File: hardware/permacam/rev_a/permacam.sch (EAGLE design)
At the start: 89 parts, among them J1 TC2030-JLINK-NL, Q1 PMDXB950UPEL, Q3 PMDXB950UPEL, Q5 PMDXB950UPEL, Q6 PMDXB950UPEL, U1 AB1815-T3, U10 NRF52840, U2 BQ25505, U3 EKMB1101111, U4 HM01B0-ANA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

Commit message: clean and orient design blocks
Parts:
- added C17, C18, C19: 0.1uF, passives:CAPACITOR0402_CAP
- added C20: 10uF, passives:CAPACITOR0603_CAP
- added R5, R6: 1k, passives:RESISTOR0402_RES
- added U5: MCP1810, chips:MCP1810
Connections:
- new net !CAM_EN: U5.!SHDN
- new net CAM_D0: U10.P0.22, U4.D0
- new net CAM_D1: U4.D1
- new net CAM_D2: U4.D2
- new net CAM_D3: U4.D3
- new net CAM_INT: U10.P1.03, U4.INT
- new net CAM_SCL: U10.P0.11
- new net CAM_SDA: R5.2, R6.2, U10.P0.07, U4.SCL, U4.SDA
- new net CAM_TRIG: U10.P1.02, U4.TRIG
- new net FVLD: U10.P0.24, U4.FVLD
- new net LVLD: U10.P0.23, U4.LVLD
- new net MCLK: U10.P0.20, U4.MCLK
- new net PCLKO: U10.P0.21, U4.PCLKO
- new net VCC28: C17.1, C18.1, C19.1, C20.1, R5.1, R6.1, U4.AVDD, U4.DVDD, U4.IOVDD, U5.VOUT
- net !LT_EN: now also U10.P1.01; no longer U10.P0.24
- net GND: now also C17.2, C18.2, C19.2, C20.2, U4.GND, U5.GND
- net VCC: now also U5.VIN
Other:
- moved on the sheet: U4

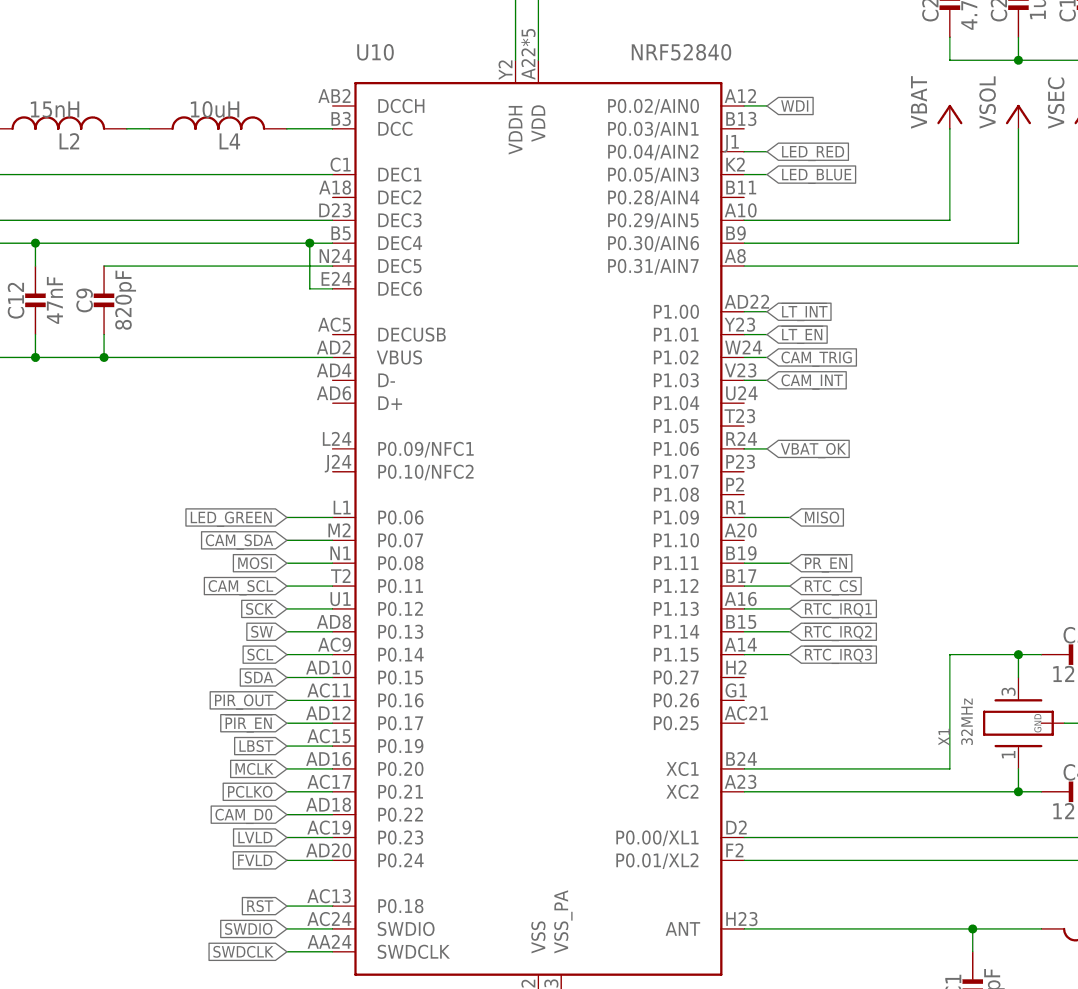
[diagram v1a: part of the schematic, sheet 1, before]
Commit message: Route signals on board - no airwires or major drc
Need to add optional MSP430
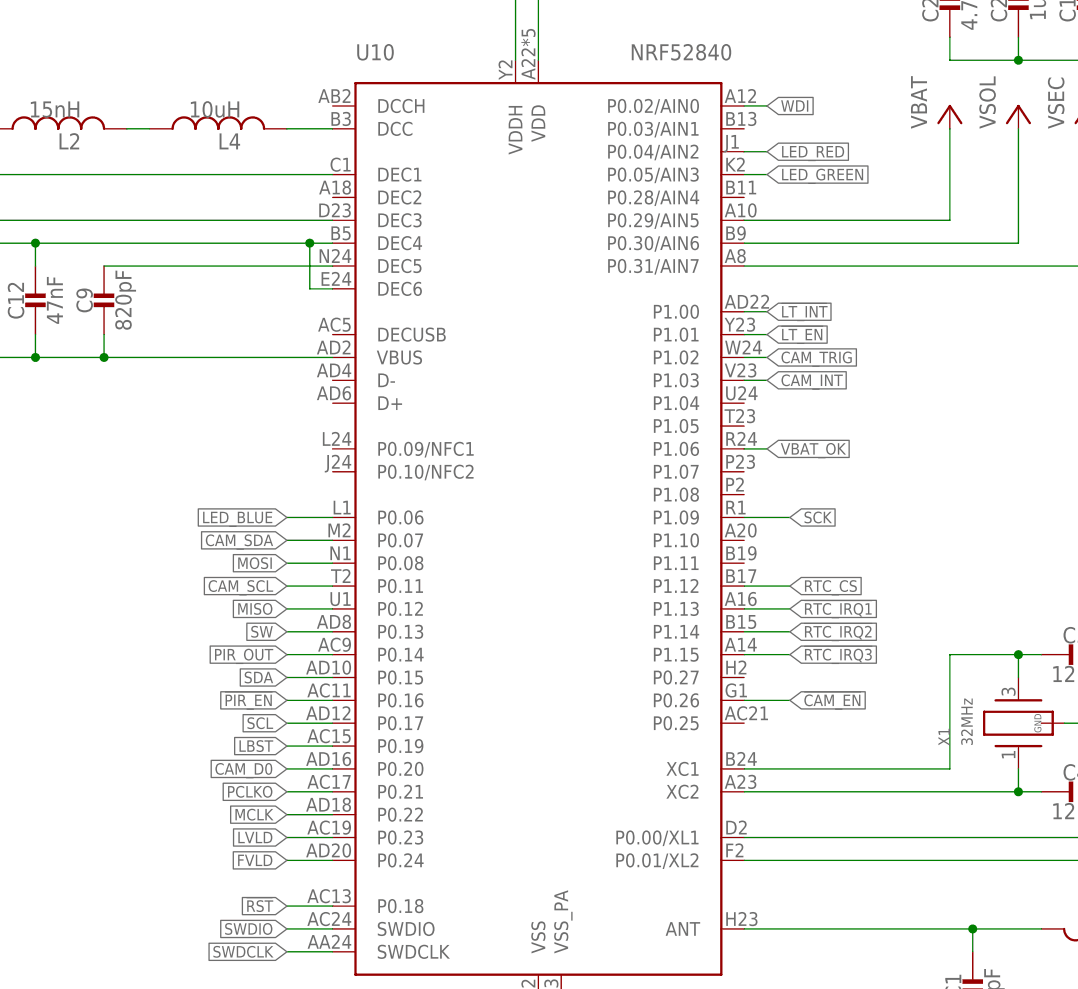
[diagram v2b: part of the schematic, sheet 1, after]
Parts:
- removed TP24: TEST-POINT, headers:TEST-POINT
- added TP7: TEST-POINT, headers:TEST-POINT
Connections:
- removed net !PR_EN: U10.P1.11
- net !CAM_EN: now also U10.P0.26
- net !PIR_EN: now also U10.P0.16; no longer U10.P0.17
- net CAM_D0: now also U10.P0.20; no longer U10.P0.22
- net CAM_SCL: now also R5.2, U4.SCL
- net CAM_SDA: no longer R5.2, U4.SCL
- net LED_BLUE: now also U10.P0.06; no longer U10.P0.05/AIN3
- net LED_GREEN: now also U10.P0.05/AIN3; no longer U10.P0.06
- net MCLK: now also U10.P0.22; no longer U10.P0.20
- net MISO: now also U10.P0.12; no longer U10.P1.09
- net PIR_OUT: now also U10.P0.14; no longer U10.P0.16
- net SCK: now also U10.P1.09; no longer U10.P0.12
- net SCL: now also U10.P0.17; no longer U10.P0.14
- net VCC28: now also TP7.TESTPOINT
- net VSEC: no longer TP24.TESTPOINT
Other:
- moved on the sheet: TP25

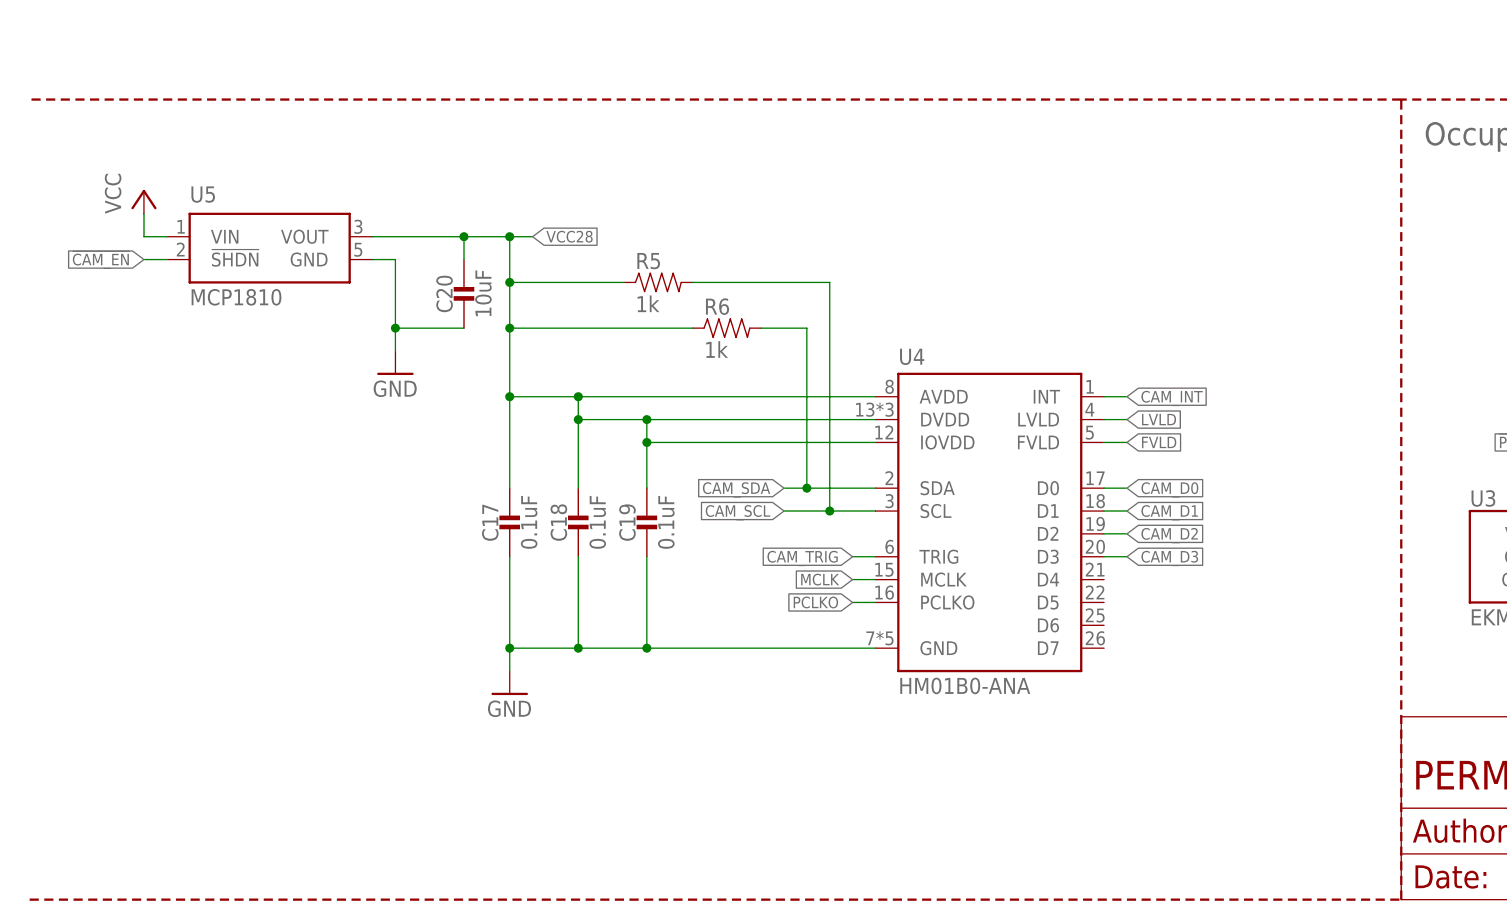
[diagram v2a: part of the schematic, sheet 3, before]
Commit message: Rearrange pin assignments to match board locations
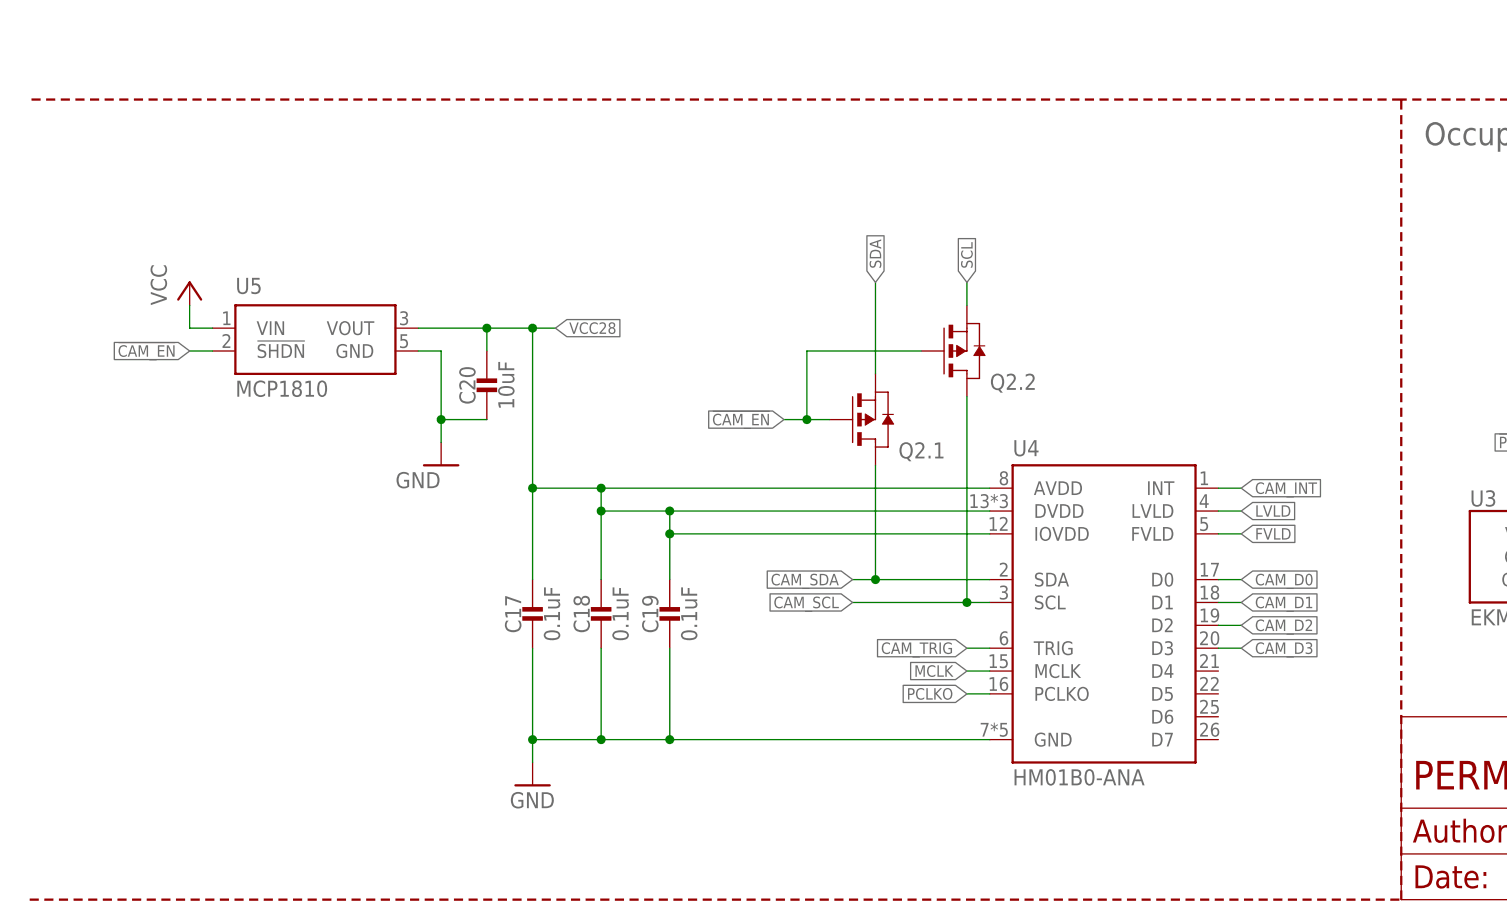
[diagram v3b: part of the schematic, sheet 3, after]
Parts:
- removed R5, R6: 1k, passives:RESISTOR0402_RES
- added Q2: PMDXB950UPEL, fets:PMDXB950UPEL
- added R7, R8: 1k, passives:RESISTOR0402_RES
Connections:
- net !CAM_EN: now also Q2.1.G, Q2.2.G, U10.P0.20; no longer U10.P0.26
- net !LT_EN: now also U10.P0.28/AIN4; no longer U10.P1.01
- net !LT_INT: now also U10.P0.03/AIN1; no longer U10.P1.00
- net !PIR_EN: now also U10.P1.11; no longer U10.P0.16
- net !RTC_IRQ2: now also U10.P1.15; no longer U10.P1.14
- net !RTC_IRQ3: now also U10.P1.14; no longer U10.P1.15
- net CAM_D0: now also U10.P0.15; no longer U10.P0.20
- net CAM_D1: now also U10.P0.16
- net CAM_D2: now also U10.P0.17
- net CAM_D3: now also U10.P0.19
- net CAM_SCL: now also Q2.2.D; no longer R5.2, U10.P0.11
- net CAM_SDA: now also Q2.1.D; no longer R6.2, U10.P0.07
- net LBST: now also U10.P0.12; no longer U10.P0.19
- net LED_BLUE: now also U10.P0.04/AIN2; no longer U10.P0.06
- net LED_RED: now also U10.P0.27; no longer U10.P0.04/AIN2
- net MISO: now also U10.P0.08; no longer U10.P0.12
- net MOSI: now also U10.P0.06; no longer U10.P0.08
- net PIR_OUT: now also U10.P1.10; no longer U10.P0.14
- net SCK: now also U10.P0.07; no longer U10.P1.09
- net SCL: now also Q2.2.S, R8.1, U10.P0.14; no longer U10.P0.17
- net SDA: now also Q2.1.S, R7.1, U10.P0.13; no longer U10.P0.15
- net SW: now also U10.P1.09; no longer U10.P0.13
- net VBAT_OK: now also U10.P0.11; no longer U10.P1.06
- net VCC28: now also R7.2, R8.2; no longer R5.1, R6.1
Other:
- note removed: "Note: Only populate one type of battery holder"
- moved on the sheet: C17, C18, C19, C20, U4, U5

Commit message: Use serial data + one vcc at 2.8V
Need to divide primary cell voltage for sensing
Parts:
- removed C20: 10uF, passives:CAPACITOR0603_CAP
- removed R7, R8: 1k, passives:RESISTOR0402_RES
- removed TP7: TEST-POINT, headers:TEST-POINT
- removed U5: MCP1810, chips:MCP1810
- added Q4: PMDXB950UPEL, fets:PMDXB950UPEL
- added R5: 100M, passives:RESISTOR0402_RES
- added U6: SN74AUP2G04DCKRDCK6-L, chips:SN74AUP2G04DCKRDCK6-L
- R13: value 80.6k -> 215k
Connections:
- removed net VCC28: C17.1, C18.1, C19.1, C20.1, R7.2, R8.2, TP7.TESTPOINT, U4.AVDD, U4.DVDD, U4.IOVDD, U5.VOUT
- new net !FVLD: U4.FVLD, U6.1A
- new net !LVLD: U4.LVLD, U6.2A
- new net N$16: C17.1, C18.1, C19.1, Q4.1.D, U4.AVDD, U4.DVDD, U4.IOVDD, U6.VCC
- net !CAM_EN: now also Q4.1.G, R5.1, U10.P0.15; no longer U10.P0.20, U5.!SHDN
- net CAM_D0: now also U10.P0.17; no longer U10.P0.15
- net CAM_D1: no longer U10.P0.16
- net CAM_D2: no longer U10.P0.17
- net CAM_D3: no longer U10.P0.19
- net CAM_INT: now also U10.P0.25; no longer U10.P1.03
- net CAM_TRIG: now also U10.P0.23; no longer U10.P1.02
- net FVLD: now also U6.1Y; no longer U4.FVLD
- net GND: now also U6.GND; no longer C20.2, U5.GND
- net LVLD: now also U10.P1.00, U6.2Y; no longer U10.P0.23, U4.LVLD
- net PCLKO: now also U10.P0.20; no longer U10.P0.21
- net SCL: no longer R8.1
- net SDA: no longer R7.1
- net VCC: now also Q4.1.S, R5.2; no longer U5.VIN
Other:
- moved on the sheet: C17, C18, C19, Q2.1, Q2.2, U4

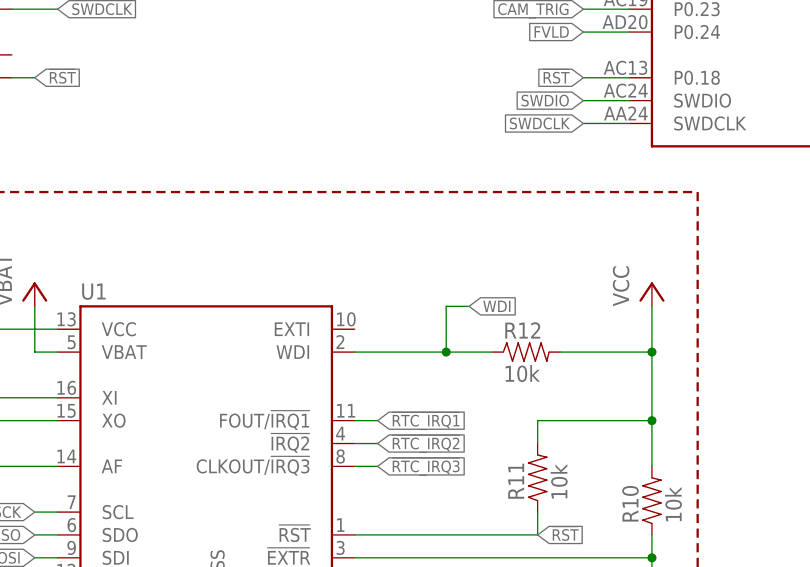
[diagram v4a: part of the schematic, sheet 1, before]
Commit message: fix exti floating
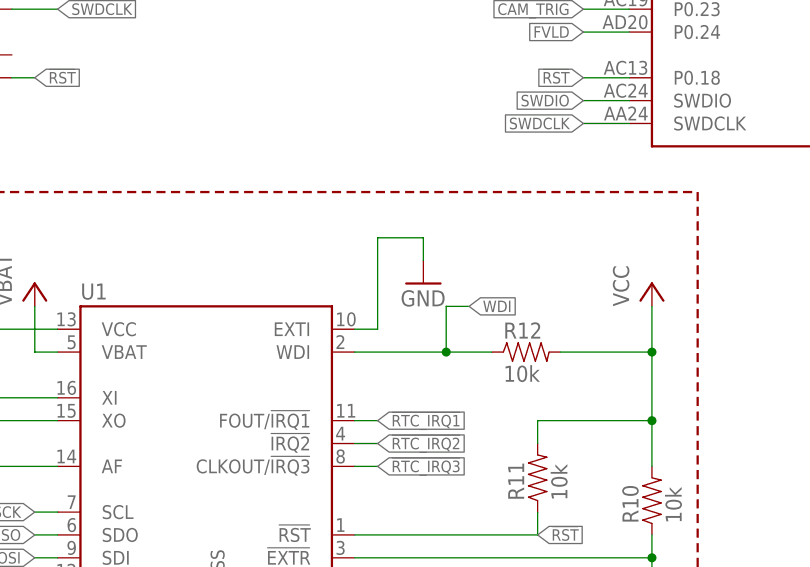
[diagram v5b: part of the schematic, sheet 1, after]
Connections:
- net GND: now also U1.EXTI
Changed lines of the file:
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@@
 <?xml version="1.0" encoding="utf-8"?>
 <!DOCTYPE eagle SYSTEM "eagle.dtd">
-<eagle version="9.4.2">
+<eagle version="9.5.1">
 <drawing>
 <settings>
@@
 <attribute name="MPN" value="HMC0402JT100M "/>
 </part>
+<part name="GND7" library="supply1" library_urn="urn:adsk.eagle:library:371" deviceset="GND" device=""/>
 </parts>
 <sheets>
@@
 <instance part="S1" gate="G$1" x="88.9" y="7.62" smashed="yes">
 <attribute name="NAME" x="86.36" y="5.08" size="1.778" layer="95"/>
+</instance>
+<instance part="GND7" gate="1" x="91.44" y="48.26" smashed="yes">
+<attribute name="VALUE" x="88.9" y="45.72" size="1.778" layer="96"/>
 </instance>
 </instances>
@@
 <wire x1="226.06" y1="76.2" x2="223.52" y2="76.2" width="0.1524" layer="91"/>
 </segment>
+<segment>
+<pinref part="U1" gate="G$1" pin="EXTI"/>
+<wire x1="83.82" y1="43.18" x2="86.36" y2="43.18" width="0.1524" layer="91"/>
+<wire x1="86.36" y1="43.18" x2="86.36" y2="53.34" width="0.1524" layer="91"/>
+<wire x1="86.36" y1="53.34" x2="91.44" y2="53.34" width="0.1524" layer="91"/>
+<wire x1="91.44" y1="53.34" x2="91.44" y2="50.8" width="0.1524" layer="91"/>
+<pinref part="GND7" gate="1" pin="GND"/>
+</segment>
 </net>
